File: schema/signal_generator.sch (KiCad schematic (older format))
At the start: 20 parts

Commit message: reannotate schema
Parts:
- gave numbers to parts that had none: 8
- renumbered 1.5k to 1.5k1, 100nF to 100nF1, 11.5k to 11.5k1, 433k to 433k1, 577k to 577k1
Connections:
- net GND: now also U9.6, U9.9; no longer U9.1, U9.2
- net OUTPUT: now also U9.11; no longer U9.3
- net at U6.4 (~RESET): now also U9.4; no longer U9.3
- net at U9.3: now also U9.8; no longer U9.1
- new net: U10.12 (TC), U9.12, U9.5
- new net: U9.10, U9.13
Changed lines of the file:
@@
 $Descr A4 11693 8268
 encoding utf-8
-Sheet 2 6
+Sheet 6 6
 Title ""
 Date ""
@@
 $EndDescr
 $Comp
-L HEF4526B U?
+L HEF4526B U10
 U 1 1 5912CAA9
 P 6550 3850
-F 0 "U?" H 6950 3250 60  0000 C CNN
+F 0 "U10" H 6950 3250 60  0000 C CNN
 F 1 "HEF4526B" H 6800 3350 60  0000 C CNN
 F 2 "" H 6550 3850 60  0001 C CNN
@@
 $EndComp
 $Comp
-L TLC555 U?
+L TLC555 U5
 U 1 1 5912CB7D
 P 2000 2950
-F 0 "U?" H 1900 3375 50  0000 R CNN
+F 0 "U5" H 1900 3375 50  0000 R CNN
 F 1 "TLC555" H 1900 3300 50  0000 R CNN
 F 2 "" H 2050 2700 50  0000 L CNN
@@
 $EndComp
 $Comp
-L +BATT #PWR?
+L +BATT #PWR49
 U 1 1 5912CCA8
 P 6750 1050
-F 0 "#PWR?" H 6750 900 50  0001 C CNN
+F 0 "#PWR49" H 6750 900 50  0001 C CNN
 F 1 "+BATT" H 6750 1190 50  0000 C CNN
 F 2 "" H 6750 1050 50  0000 C CNN
@@
 NoConn ~ 7150 4050
 $Comp
-L SW_DIP_x4 S?
+L SW_DIP_x4 S2
 U 1 1 5912E74A
 P 6750 1600
-F 0 "S?" H 6750 1350 50  0000 C CNN
+F 0 "S2" H 6750 1350 50  0000 C CNN
 F 1 "SW_DIP_x4" H 6750 1850 50  0000 C CNN
 F 2 "" H 6700 1600 50  0000 C CNN
@@
 $EndComp
 $Comp
-L GND #PWR?
+L GND #PWR50
 U 1 1 5912ED7F
 P 7600 3000
-F 0 "#PWR?" H 7600 2750 50  0001 C CNN
+F 0 "#PWR50" H 7600 2750 50  0001 C CNN
 F 1 "GND" H 7600 2850 50  0000 C CNN
 F 2 "" H 7600 3000 50  0000 C CNN
@@
 $EndComp
 $Comp
-L GND #PWR?
+L GND #PWR48
 U 1 1 59130203
 P 6450 4700
-F 0 "#PWR?" H 6450 4450 50  0001 C CNN
+F 0 "#PWR48" H 6450 4450 50  0001 C CNN
 F 1 "GND" H 6450 4550 50  0000 C CNN
 F 2 "" H 6450 4700 50  0000 C CNN
@@
 $EndComp
 $Comp
-L +BATT #PWR?
+L +BATT #PWR46
 U 1 1 591303F3
 P 6250 3250
-F 0 "#PWR?" H 6250 3100 50  0001 C CNN
+F 0 "#PWR46" H 6250 3100 50  0001 C CNN
 F 1 "+BATT" H 6250 3390 50  0000 C CNN
 F 2 "" H 6250 3250 50  0000 C CNN
@@
 $EndComp
 $Comp
-L +BATT #PWR?
+L +BATT #PWR41
 U 1 1 591329F1
 P 2000 1950
-F 0 "#PWR?" H 2000 1800 50  0001 C CNN
+F 0 "#PWR41" H 2000 1800 50  0001 C CNN
 F 1 "+BATT" H 2000 2090 50  0000 C CNN
 F 2 "" H 2000 1950 50  0000 C CNN
@@
 $EndComp
 $Comp
-L R 433k
+L R 433k1
 U 1 1 59132C26
 P 1050 3000
-F 0 "433k" V 1130 3000 50  0000 C CNN
+F 0 "433k1" V 1130 3000 50  0000 C CNN
 F 1 "467k" V 1050 3000 50  0000 C CNN
 F 2 "" V 980 3000 50  0000 C CNN
@@
 $EndComp
 $Comp
-L R R?
+L R R13
 U 1 1 59132D4D
 P 2950 2450
-F 0 "R?" V 3030 2450 50  0000 C CNN
+F 0 "R13" V 3030 2450 50  0000 C CNN
 F 1 "R" V 2950 2450 50  0000 C CNN
 F 2 "" V 2880 2450 50  0000 C CNN
@@
 $EndComp
 $Comp
-L GND #PWR?
+L GND #PWR42
 U 1 1 59132E59
 P 2000 3700
-F 0 "#PWR?" H 2000 3450 50  0001 C CNN
+F 0 "#PWR42" H 2000 3450 50  0001 C CNN
 F 1 "GND" H 2000 3550 50  0000 C CNN
 F 2 "" H 2000 3700 50  0000 C CNN
@@
 NoConn ~ 2500 3050
 $Comp
-L R 577k
+L R 577k1
 U 1 1 59133297
 P 1050 2500
-F 0 "577k" V 1130 2500 50  0000 C CNN
+F 0 "577k1" V 1130 2500 50  0000 C CNN
 F 1 "556k" V 1050 2500 50  0000 C CNN
 F 2 "" V 980 2500 50  0000 C CNN
@@
 $EndComp
 $Comp
-L C C?
+L C C10
 U 1 1 5913391D
 P 1450 3450
-F 0 "C?" H 1475 3550 50  0000 L CNN
+F 0 "C10" H 1475 3550 50  0000 L CNN
 F 1 "C" H 1475 3350 50  0000 L CNN
 F 2 "" H 1488 3300 50  0000 C CNN
@@
 Decounter
 $Comp
-L TLC555 U?
+L TLC555 U6
 U 1 1 5913C644
 P 2000 5850
-F 0 "U?" H 1900 6275 50  0000 R CNN
+F 0 "U6" H 1900 6275 50  0000 R CNN
 F 1 "TLC555" H 1900 6200 50  0000 R CNN
 F 2 "" H 2050 5600 50  0000 L CNN
@@
 $EndComp
 $Comp
-L +BATT #PWR?
+L +BATT #PWR43
 U 1 1 5913C64A
 P 2000 4850
-F 0 "#PWR?" H 2000 4700 50  0001 C CNN
+F 0 "#PWR43" H 2000 4700 50  0001 C CNN
 F 1 "+BATT" H 2000 4990 50  0000 C CNN
 F 2 "" H 2000 4850 50  0000 C CNN
@@
 $EndComp
 $Comp
-L R 1.5k
+L R 1.5k1
 U 1 1 5913C657
 P 1050 5900
-F 0 "1.5k" V 1130 5900 50  0000 C CNN
+F 0 "1.5k1" V 1130 5900 50  0000 C CNN
 F 1 "R" V 1050 5900 50  0000 C CNN
 F 2 "" V 980 5900 50  0000 C CNN
@@
 $EndComp
 $Comp
-L R RL?
+L R RL5
 U 1 1 5913C665
 P 2950 5350
-F 0 "RL?" V 3030 5350 50  0000 C CNN
+F 0 "RL5" V 3030 5350 50  0000 C CNN
 F 1 "R" V 2950 5350 50  0000 C CNN
 F 2 "" V 2880 5350 50  0000 C CNN
@@
 $EndComp
 $Comp
-L GND #PWR?
+L GND #PWR44
 U 1 1 5913C66F
 P 2000 6600
-F 0 "#PWR?" H 2000 6350 50  0001 C CNN
+F 0 "#PWR44" H 2000 6350 50  0001 C CNN
 F 1 "GND" H 2000 6450 50  0000 C CNN
 F 2 "" H 2000 6600 50  0000 C CNN
@@
 NoConn ~ 2500 5950
 $Comp
-L R 11.5k
+L R 11.5k1
 U 1 1 5913C678
 P 1050 5400
-F 0 "11.5k" V 1130 5400 50  0000 C CNN
+F 0 "11.5k1" V 1130 5400 50  0000 C CNN
 F 1 "12k" V 1050 5400 50  0000 C CNN
 F 2 "" V 980 5400 50  0000 C CNN
@@
 $EndComp
 $Comp
-L C 100nF
+L C 100nF1
 U 1 1 5913C686
 P 1450 6350
-F 0 "100nF" H 1475 6450 50  0000 L CNN
+F 0 "100nF1" H 1475 6450 50  0000 L CNN
 F 1 "C" H 1475 6250 50  0000 L CNN
 F 2 "" H 1488 6200 50  0000 C CNN
@@
 P 5300 5400
 AR Path="/591D57A6" Ref="U?"  Part="1"
-AR Path="/5910364F/591D57A6" Ref="U?"  Part="1"
-F 0 "U?" H 5300 5450 50  0000 C CNN
+AR Path="/5910364F/591D57A6" Ref="U9"  Part="1"
+F 0 "U9" H 5300 5450 50  0000 C CNN
 F 1 "7402" H 5350 5350 50  0000 C CNN
 F 2 "" H 5300 5400 50  0000 C CNN
@@
 $Comp
 L 7402-RESCUE-IRemote U?
-U 1 1 591D7115
+U 3 1 591D7115
 P 6700 5500
 AR Path="/591D7115" Ref="U?"  Part="1"
-AR Path="/5910364F/591D7115" Ref="U?"  Part="1"
-F 0 "U?" H 6700 5550 50  0000 C CNN
+AR Path="/5910364F/591D7115" Ref="U9"  Part="3"
+F 0 "U9" H 6700 5550 50  0000 C CNN
 F 1 "7402" H 6750 5450 50  0000 C CNN
 F 2 "" H 6700 5500 50  0000 C CNN
 F 3 "" H 6700 5500 50  0000 C CNN
-	1    6700 5500
-	1    0    0    -1
-$EndComp
-$Comp
-L GND #PWR?
+	3    6700 5500
+	1    0    0    -1
+$EndComp
+$Comp
+L GND #PWR45
 U 1 1 591D7268
 P 5950 5750
-F 0 "#PWR?" H 5950 5500 50  0001 C CNN
+F 0 "#PWR45" H 5950 5500 50  0001 C CNN
 F 1 "GND" H 5950 5600 50  0000 C CNN
 F 2 "" H 5950 5750 50  0000 C CNN
@@
 $Comp
 L 7402-RESCUE-IRemote U?
-U 1 1 591D774A
+U 4 1 591D774A
 P 8800 5400
 AR Path="/591D774A" Ref="U?"  Part="1"
-AR Path="/5910364F/591D774A" Ref="U?"  Part="1"
-F 0 "U?" H 8800 5450 50  0000 C CNN
+AR Path="/5910364F/591D774A" Ref="U9"  Part="4"
+F 0 "U9" H 8800 5450 50  0000 C CNN
 F 1 "7402" H 8850 5350 50  0000 C CNN
 F 2 "" H 8800 5400 50  0000 C CNN
 F 3 "" H 8800 5400 50  0000 C CNN
-	1    8800 5400
+	4    8800 5400
 	1    0    0    -1
 $EndComp
@@
 	2500 2750 2700 2750
 Wire Wire Line
-	2700 2100 2700 2750
+	2700 2750 2700 2100
 Wire Wire Line
 	1050 2100 2950 2100
@@
 $Comp
 L 7402-RESCUE-IRemote U?
-U 1 1 591D82E2
+U 2 1 591D82E2
 P 5550 6450
 AR Path="/591D82E2" Ref="U?"  Part="1"
-AR Path="/5910364F/591D82E2" Ref="U?"  Part="1"
-F 0 "U?" H 5550 6500 50  0000 C CNN
+AR Path="/5910364F/591D82E2" Ref="U9"  Part="2"
+F 0 "U9" H 5550 6500 50  0000 C CNN
 F 1 "7402" H 5600 6400 50  0000 C CNN
 F 2 "" H 5550 6450 50  0000 C CNN
 F 3 "" H 5550 6450 50  0000 C CNN
-	1    5550 6450
+	2    5550 6450
 	-1   0    0    1
 $EndComp
@@
 Connection ~ 7900 5300
 $Comp
-L GND #PWR?
+L GND #PWR47
 U 1 1 591DA0C5
 P 6300 6700
-F 0 "#PWR?" H 6300 6450 50  0001 C CNN
+F 0 "#PWR47" H 6300 6450 50  0001 C CNN
 F 1 "GND" H 6300 6550 50  0000 C CNN
 F 2 "" H 6300 6700 50  0000 C CNN

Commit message: update some ref in signal gen
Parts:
- Cp: renamed from 100nF1; value C -> 100nF
- renumbered 577k1 to Rba, 433k1 to Rbb, R13 to Rbl, 11.5k1 to Rpa, 1.5k1 to Rpb, RL5 to Rpl
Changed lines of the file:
@@
 $EndComp
 $Comp
-L R 433k1
+L R Rbb
 U 1 1 59132C26
 P 1050 3000
-F 0 "433k1" V 1130 3000 50  0000 C CNN
+F 0 "Rbb" V 1130 3000 50  0000 C CNN
 F 1 "467k" V 1050 3000 50  0000 C CNN
 F 2 "" V 980 3000 50  0000 C CNN
@@
 $EndComp
 $Comp
-L R R13
+L R Rbl
 U 1 1 59132D4D
 P 2950 2450
-F 0 "R13" V 3030 2450 50  0000 C CNN
+F 0 "Rbl" V 3030 2450 50  0000 C CNN
 F 1 "R" V 2950 2450 50  0000 C CNN
 F 2 "" V 2880 2450 50  0000 C CNN
@@
 NoConn ~ 2500 3050
 $Comp
-L R 577k1
+L R Rba
 U 1 1 59133297
 P 1050 2500
-F 0 "577k1" V 1130 2500 50  0000 C CNN
+F 0 "Rba" V 1130 2500 50  0000 C CNN
 F 1 "556k" V 1050 2500 50  0000 C CNN
 F 2 "" V 980 2500 50  0000 C CNN
@@
 $EndComp
 $Comp
-L R 1.5k1
+L R Rpb
 U 1 1 5913C657
 P 1050 5900
-F 0 "1.5k1" V 1130 5900 50  0000 C CNN
+F 0 "Rpb" V 1130 5900 50  0000 C CNN
 F 1 "R" V 1050 5900 50  0000 C CNN
 F 2 "" V 980 5900 50  0000 C CNN
@@
 $EndComp
 $Comp
-L R RL5
+L R Rpl
 U 1 1 5913C665
 P 2950 5350
-F 0 "RL5" V 3030 5350 50  0000 C CNN
+F 0 "Rpl" V 3030 5350 50  0000 C CNN
 F 1 "R" V 2950 5350 50  0000 C CNN
 F 2 "" V 2880 5350 50  0000 C CNN
@@
 NoConn ~ 2500 5950
 $Comp
-L R 11.5k1
+L R Rpa
 U 1 1 5913C678
 P 1050 5400
-F 0 "11.5k1" V 1130 5400 50  0000 C CNN
+F 0 "Rpa" V 1130 5400 50  0000 C CNN
 F 1 "12k" V 1050 5400 50  0000 C CNN
 F 2 "" V 980 5400 50  0000 C CNN
@@
 $EndComp
 $Comp
-L C 100nF1
+L C Cp
 U 1 1 5913C686
 P 1450 6350
-F 0 "100nF1" H 1475 6450 50  0000 L CNN
-F 1 "C" H 1475 6250 50  0000 L CNN
+F 0 "Cp" H 1475 6450 50  0000 L CNN
+F 1 "100nF" H 1475 6250 50  0000 L CNN
 F 2 "" H 1488 6200 50  0000 C CNN
 F 3 "" H 1450 6350 50  0000 C CNN

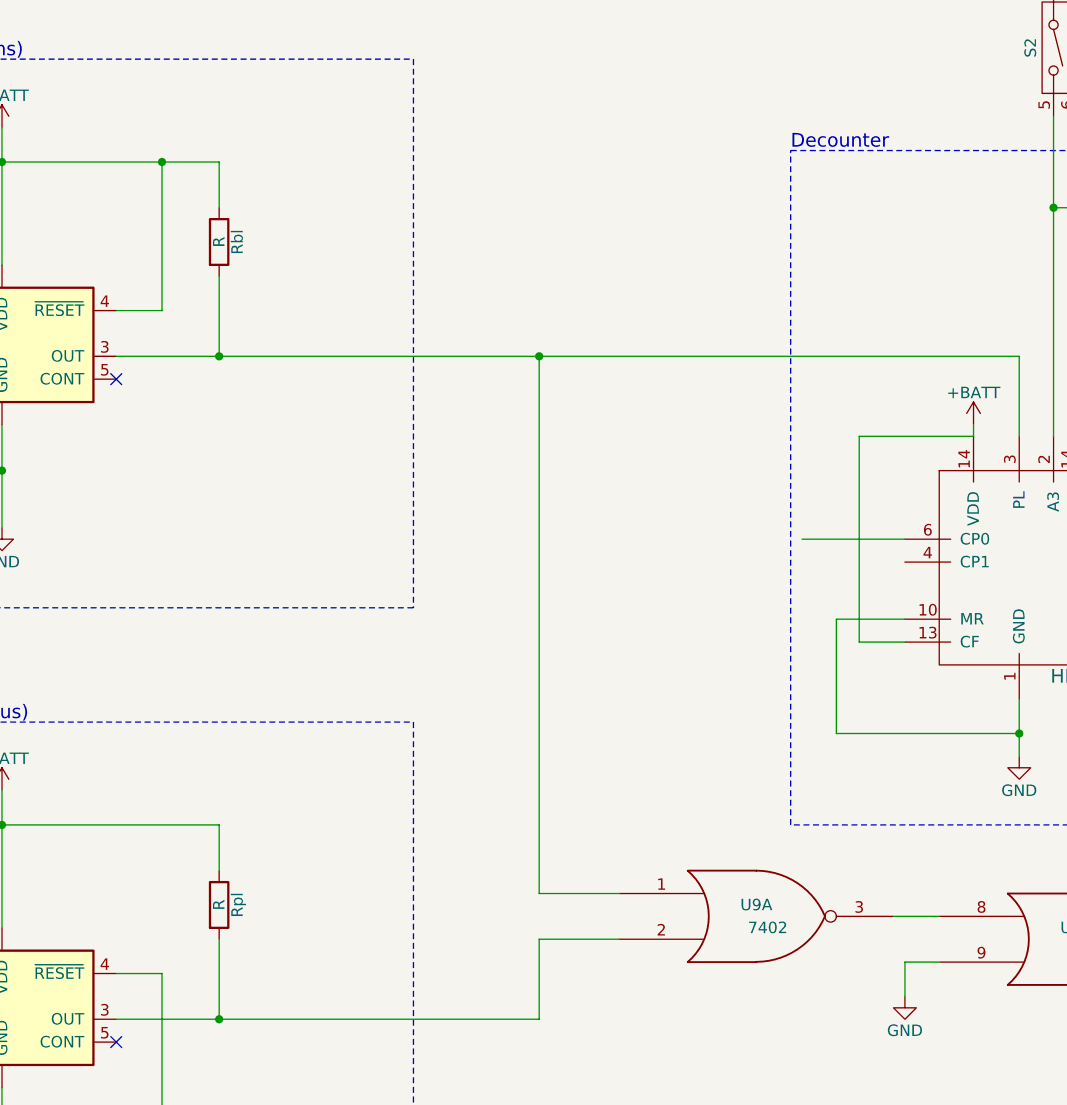
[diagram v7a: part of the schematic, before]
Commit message: Kicad signal generator
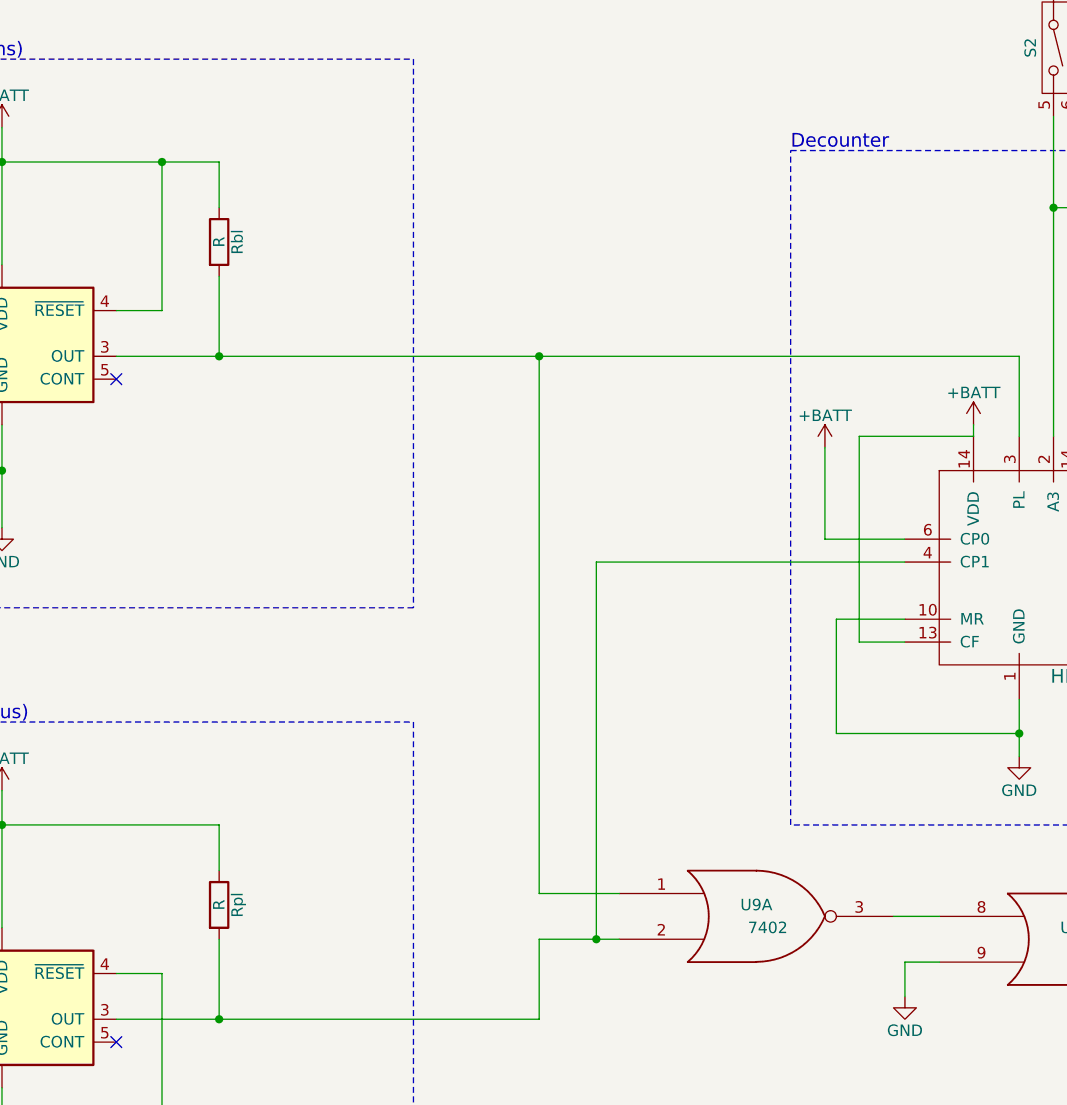
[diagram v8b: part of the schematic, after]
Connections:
- net +BATT: now also U10.6 (CP0)
- net at U10.4 (CP1): now also Rpl.2, U6.3 (OUT), U9.2
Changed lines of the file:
@@
 	2500 2950 6450 2950
-Wire Wire Line
-	5950 3750 5500 3750
 Wire Wire Line
 	5950 4100 5650 4100
@@
 	2500 2750 2700 2750
 Wire Wire Line
-	2700 2750 2700 2100
+	2700 2100 2700 2750
 Wire Wire Line
 	1050 2100 2950 2100
@@
 Wire Wire Line
 	9400 5400 10100 5400
+$Comp
+L +BATT #PWR?
+U 1 1 593EF96A
+P 5600 3350
+F 0 "#PWR?" H 5600 3200 50  0001 C CNN
+F 1 "+BATT" H 5600 3490 50  0000 C CNN
+F 2 "" H 5600 3350 50  0000 C CNN
+F 3 "" H 5600 3350 50  0000 C CNN
+	1    5600 3350
+	1    0    0    -1
+$EndComp
+Wire Wire Line
+	5600 3350 5600 3750
+Wire Wire Line
+	5600 3750 5950 3750
+Wire Wire Line
+	4600 5500 4600 3850
+Wire Wire Line
+	4600 3850 5950 3850
+Connection ~ 4600 5500
 $EndSCHEMATC
